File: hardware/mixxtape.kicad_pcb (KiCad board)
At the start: 2 copper layers, 100.3 x 63.5 mm, 71 parts, among them J1 USB-C_SMD-TYPE-C-31-M-12_1, J4 TF-SMD_TF-01A, J5 PROG_JIG, SW1 SW-SMD_4P-L5.1-W5.1-P3.70-LS6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, SW2 SW-SMD_4P-L5.1-W5.1-P3.70-LS6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, SW3 SW-SMD_4P-L5.1-W5.1-P3.70-LS6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, SW4 SW-SMD_4P-L5.1-W5.1-P3.70-LS6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, U1 WIFI-SMD_ESP32-WROOM-32E, U2 LGA-8_L4.0-W3.0-R_WMM7040DT0, U3 SOIC-8_L5.3-W5.3-P1.27-LS8.0-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, U4 SOT-223-3_L6.5-W3.4-P2.30-LS7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, U8 SOT-23-5_L3.0-W1.7-P0.95-LS2.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

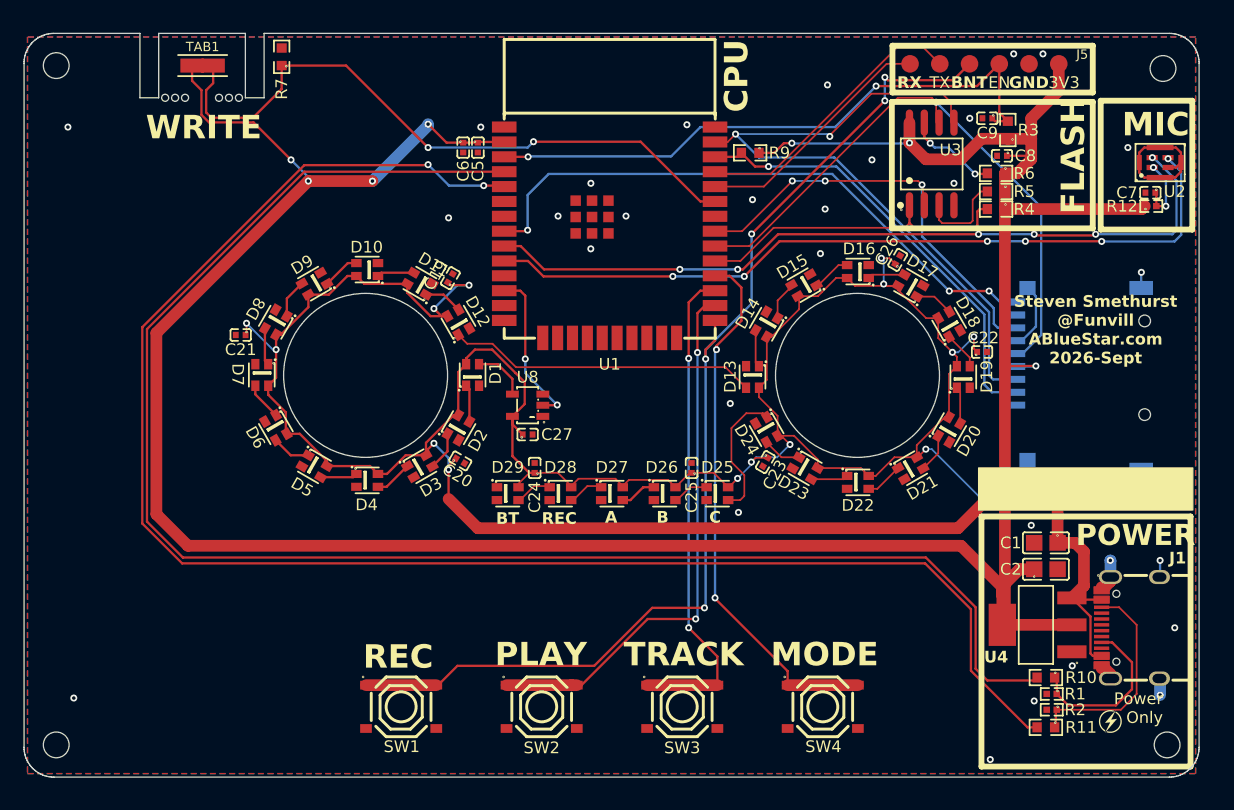
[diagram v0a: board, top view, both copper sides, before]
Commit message: hardware+firmware: flash second-sourced, passives on 0402, ERC actually clean
Flash: U3 moves from Winbond W25Q128JVSIQ (C97521) to GigaDevice
GD25Q128ESIG (C2758105), $2.2557 -> $1.3348 at a run of 20, net $15.41
after the Extended setup fee. Land patterns agree to 0.02 mm and the
command set and 256 B / 4 KiB / 64 KiB geometry are identical, so neither
the layout nor the storage design changes. The only difference is the
JEDEC manufacturer byte, so rather than move the hard-coded constant both
the driver and the factory test now accept either id and log which part
was found - C97521 stays a genuine drop-in second source. Host tests 11/11.

Passives: the eight 10k resistors move R0603 -> R0402, cheaper as well as
smaller, no traces broken. C1/C2 stay 0805 because the only Basic 10uF in
0402 is 6.3 V and C1 sits on the 5 V USB rail, where derating would leave
~2 uF of the nominal 10 for 29 LEDs.

ERC: three dangling 1.27 mm wire stubs left behind by the touch-pad
removal. These had been reported as clean because the report being read
was stale - kicad-cli writes its report relative to the working directory,
not next to the board. Both locations are now gitignored and the tracked
copy is deleted. ERC is now 0 errors, 0 warnings.

Checklist: the case-fit test passed against a real plastic case, which
retires the largest mechanical unknown. Testing against other brands stays
open. Also corrected the instruction to re-run gen_layout.py, which would
have rebuilt the original 100.33 mm outline and discarded the trim to
99.50 mm along with every route since.

fab/ now holds the JLCPCB upload package and its README.

Board cost $9.41 -> $8.62.

Co-Authored-By: Claude Opus 5 <noreply@anthropic.com>
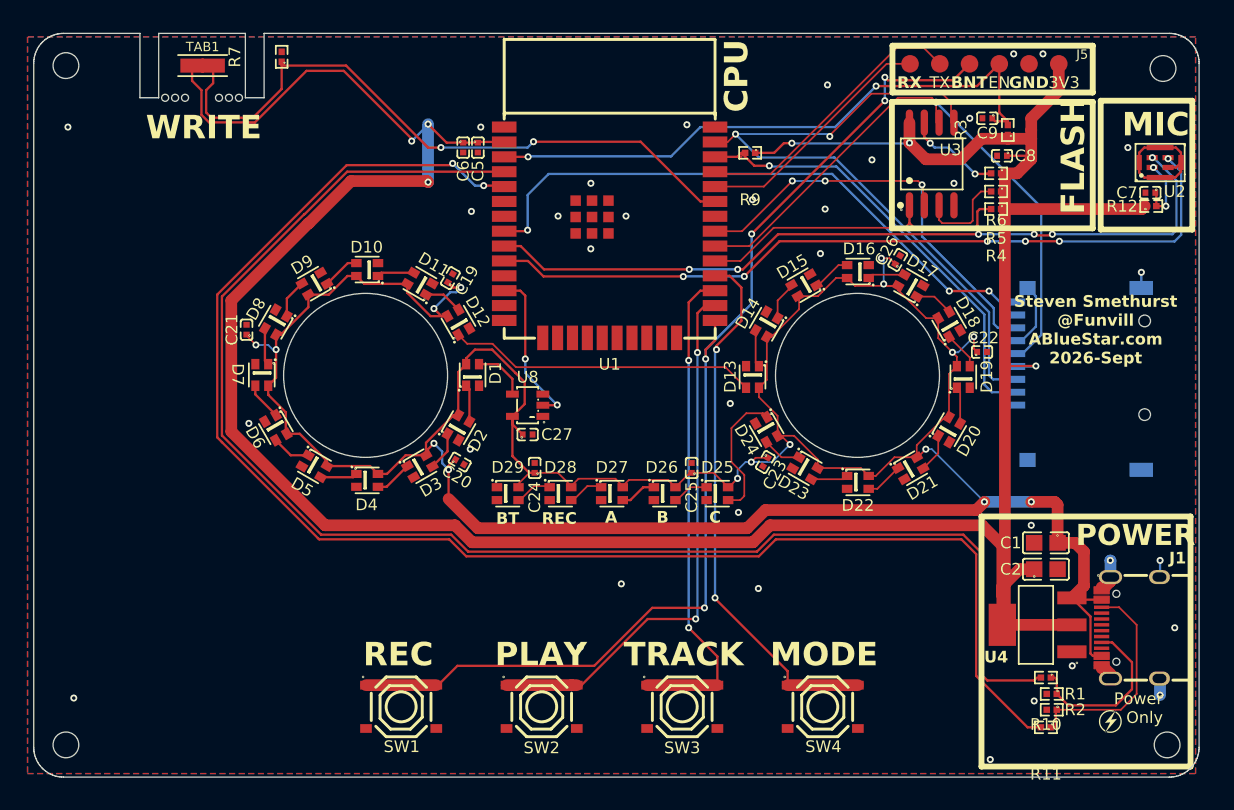
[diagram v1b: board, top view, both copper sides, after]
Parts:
- C1, C2: value C0805 -> 10uF
- R10, R11, R3, R4, R5, R6, R7, R9: footprint R0603 -> R0402
- moved C21 0.67 mm to (49.0, 55.3), turned to 90 degrees
- moved C20 0.11 mm to (67.2, 66.6)
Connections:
- U1 pad 13: unconnected-(U1-IO14-Pad13) -> (no net)
- U1 pad 16: unconnected-(U1-IO13-Pad16) -> (no net)
- U1 pad 23: unconnected-(U1-IO15-Pad23) -> (no net)
- U1 pad 24: unconnected-(U1-IO2-Pad24) -> (no net)
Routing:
- net CC1_SENSE: track 137.3 -> 126.0 mm
- net CC2_SENSE: track 140.9 -> 129.7 mm
- net 3V3: track 254.0 -> 257.9 mm, vias 7 -> 6
- net VBUS: track 268.4 -> 266.1 mm
- net GND: vias 30 -> 35
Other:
- board size 100.3 x 63.5 mm -> 99.5 x 63.5 mm

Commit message: hardware: fix a latent fatal LED footprint fault; clear 19 hidden DRC rules
The LED footprint was drawn for the GENUINE Worldsemi WS2812B-2020 (C965555)
and still carried that part number, while the BOM shipped the XINGLIGHT clone
C5349955, whose pad 1 is on the diagonally opposite corner. Every one of the
29 LEDs would have had VDD on the GND net and GND on VBUS - reverse-powered
across the 5 V rail, with no bodge possible on 0.225 mm of exposed copper.
ERC, DRC, the netlist and the BOM/CPL cross-check all passed, because every
one of them trusts the footprint.

Switched to XL-1615RGBC-2812B (C5349954), which Steven has used before: half
the price, double the stock, and its pin FUNCTIONS land in the same corners
the board already routes to, so the swap needed no re-routing - 0 unconnected.
Its pad NUMBERING is the manufacturer's (1=GND 2=DIN 3=VDD 4=DOUT), so the
symbol's pins were renumbered to match while leaving their positions and names
untouched, keeping every wire attached where it was.

J5, the only programming interface on the board, had F.Paste on all six bare
pogo pads - JLC would have stencilled solder onto them, leaving six uneven
blobs on the one path firmware can take onto a bare board. Removed, on the
board and in the library. Its silkscreen also read "BNT"; now "IO0".

Eleven DRC rules had been set to ignore or warning, hiding 144 findings.
Promoted 19 to error and fixed everything they surfaced: two dangling track
stubs, two missing courtyards, a starved thermal relief on D24, eight
hairline silk strokes at 0.06 mm that would not have printed, and text below
JLC's 1.0 mm / 0.15 mm floors. Added 7 GND stitching vias to the F.Cu ground
islands that hung off the plane by a single via, including U8's return path.
silk_edge_clearance stays a warning: the B-side art is a deliberate full
bleed and the fab clips it.

DRC 0 errors, 0 unconnected. ERC 0 errors, 0 warnings.
Board cost $8.62 -> $8.03.

Co-Authored-By: Claude Opus 5 <noreply@anthropic.com>
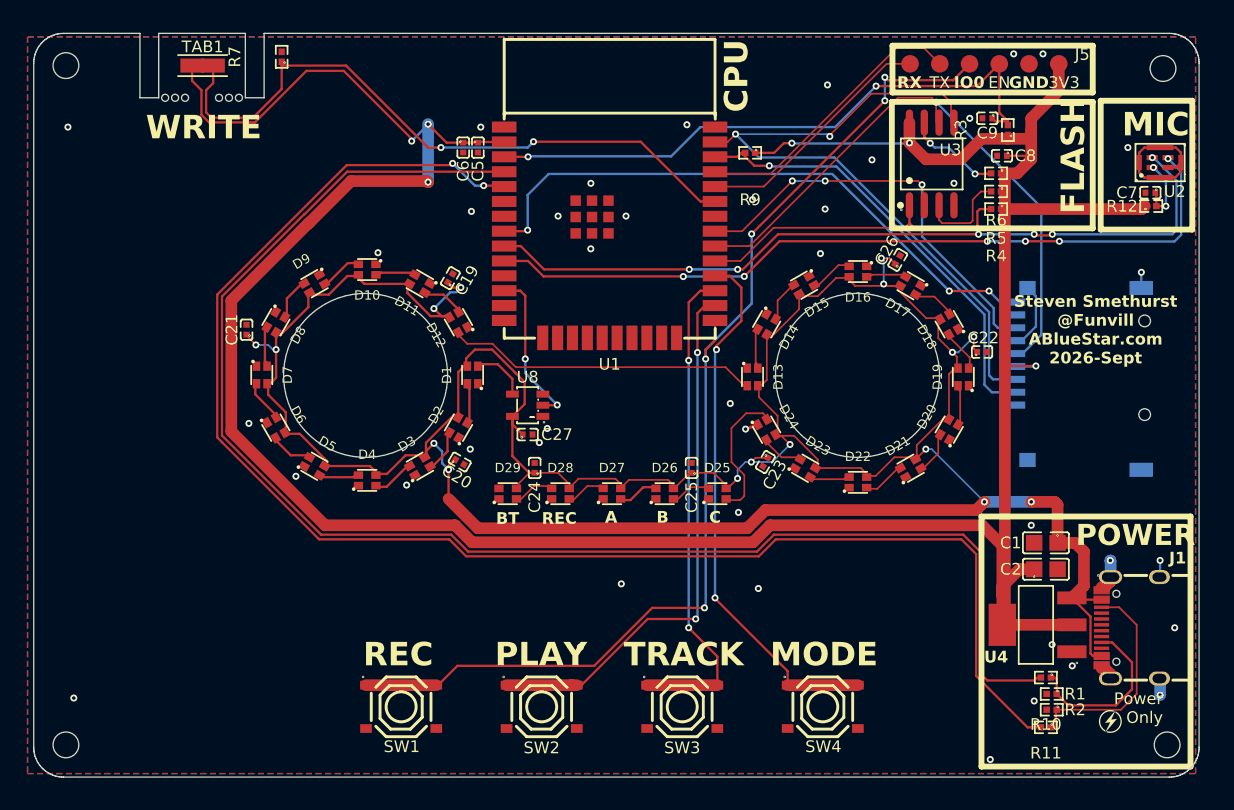
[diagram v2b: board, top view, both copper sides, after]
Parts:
- D1, D10, D11, D12, D13, D14, D15, D16, D17, D18, D19, D2, D20, D21, D22, D23, D24, D25, D26, D27, D28, D29, D3, D4, D5, D6, D7, D8, D9: value LED-SMD_4P-L2.0-W2.0-TL_WS2812B-2020 -> XL-1615RGBC-2812B; footprint LED-SMD_4P-L2.0-W2.0-TL_WS2812B-2020 -> LED-SMD_4P-L1.6-W1.5_XL-1615RGBC-2812B
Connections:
- D1 pad 1: LD1 -> GND
- D1 pad 2: GND -> LED_DATA_5V
- D1 pad 3: LED_DATA_5V -> VBUS
- D1 pad 4: VBUS -> LD1
- D10 pad 1: LD10 -> GND
- D10 pad 2: GND -> LD9
- D10 pad 3: LD9 -> VBUS
- D10 pad 4: VBUS -> LD10
- D11 pad 1: LD11 -> GND
- D11 pad 2: GND -> LD10
- D11 pad 3: LD10 -> VBUS
- D11 pad 4: VBUS -> LD11
- D12 pad 1: LD12 -> GND
- D12 pad 2: GND -> LD11
- D12 pad 3: LD11 -> VBUS
- D12 pad 4: VBUS -> LD12
- D13 pad 1: LD13 -> GND
- D13 pad 2: GND -> LD12
- D13 pad 3: LD12 -> VBUS
- D13 pad 4: VBUS -> LD13
- D14 pad 1: LD14 -> GND
- D14 pad 2: GND -> LD13
- D14 pad 3: LD13 -> VBUS
- D14 pad 4: VBUS -> LD14
- D15 pad 1: LD15 -> GND
- D15 pad 2: GND -> LD14
- D15 pad 3: LD14 -> VBUS
- D15 pad 4: VBUS -> LD15
- D16 pad 1: LD16 -> GND
- D16 pad 2: GND -> LD15
- D16 pad 3: LD15 -> VBUS
- D16 pad 4: VBUS -> LD16
- D17 pad 1: LD17 -> GND
- D17 pad 2: GND -> LD16
- D17 pad 3: LD16 -> VBUS
- D17 pad 4: VBUS -> LD17
- D18 pad 1: LD18 -> GND
- D18 pad 2: GND -> LD17
- D18 pad 3: LD17 -> VBUS
- D18 pad 4: VBUS -> LD18
- D19 pad 1: LD19 -> GND
- D19 pad 2: GND -> LD18
- D19 pad 3: LD18 -> VBUS
- D19 pad 4: VBUS -> LD19
- D2 pad 1: LD2 -> GND
- D2 pad 2: GND -> LD1
- D2 pad 3: LD1 -> VBUS
- D2 pad 4: VBUS -> LD2
- D20 pad 1: LD20 -> GND
- D20 pad 2: GND -> LD19
- D20 pad 3: LD19 -> VBUS
- D20 pad 4: VBUS -> LD20
- D21 pad 1: LD21 -> GND
- D21 pad 2: GND -> LD20
- D21 pad 3: LD20 -> VBUS
- D21 pad 4: VBUS -> LD21
- D22 pad 1: LD22 -> GND
- D22 pad 2: GND -> LD21
- D22 pad 3: LD21 -> VBUS
- D22 pad 4: VBUS -> LD22
- D23 pad 1: LD23 -> GND
- D23 pad 2: GND -> LD22
- D23 pad 3: LD22 -> VBUS
- D23 pad 4: VBUS -> LD23
- D24 pad 1: LD24 -> GND
- D24 pad 2: GND -> LD23
- D24 pad 3: LD23 -> VBUS
- D24 pad 4: VBUS -> LD24
- D25 pad 1: LD25 -> GND
- D25 pad 2: GND -> LD24
- D25 pad 3: LD24 -> VBUS
- D25 pad 4: VBUS -> LD25
- D26 pad 1: LD26 -> GND
- D26 pad 2: GND -> LD25
- D26 pad 3: LD25 -> VBUS
- D26 pad 4: VBUS -> LD26
- D27 pad 1: LD27 -> GND
- D27 pad 2: GND -> LD26
- D27 pad 3: LD26 -> VBUS
- D27 pad 4: VBUS -> LD27
- D28 pad 1: LD28 -> GND
- D28 pad 2: GND -> LD27
- D28 pad 3: LD27 -> VBUS
- D28 pad 4: VBUS -> LD28
- D29 pad 1: unconnected-(D29-DO-Pad1) -> GND
- D29 pad 2: GND -> LD28
- D29 pad 3: LD28 -> VBUS
- D29 pad 4: VBUS -> unconnected-(D29-DO-Pad1)
- D3 pad 1: LD3 -> GND
- D3 pad 2: GND -> LD2
- D3 pad 3: LD2 -> VBUS
- D3 pad 4: VBUS -> LD3
- D4 pad 1: LD4 -> GND
- D4 pad 2: GND -> LD3
- D4 pad 3: LD3 -> VBUS
- D4 pad 4: VBUS -> LD4
- D5 pad 1: LD5 -> GND
- D5 pad 2: GND -> LD4
- D5 pad 3: LD4 -> VBUS
- D5 pad 4: VBUS -> LD5
- D6 pad 1: LD6 -> GND
- D6 pad 2: GND -> LD5
- D6 pad 3: LD5 -> VBUS
- D6 pad 4: VBUS -> LD6
- D7 pad 1: LD7 -> GND
- D7 pad 2: GND -> LD6
- D7 pad 3: LD6 -> VBUS
- D7 pad 4: VBUS -> LD7
- D8 pad 1: LD8 -> GND
- D8 pad 2: GND -> LD7
- D8 pad 3: LD7 -> VBUS
- D8 pad 4: VBUS -> LD8
- D9 pad 1: LD9 -> GND
- D9 pad 2: GND -> LD8
- D9 pad 3: LD8 -> VBUS
- D9 pad 4: VBUS -> LD9
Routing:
- net GND: track 27.1 -> 28.2 mm, vias 35 -> 42
